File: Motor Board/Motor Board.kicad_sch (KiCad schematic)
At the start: 25 parts, among them J1 Programmer, J2 Gecko, J3 Gecko, J4 Conn_01x02_Socket, J5 Conn_01x02_Socket, Q1 BSS316NN, U2 PIC18F26K83, U3 MCP2562, U4 INA180

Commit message: Finish schematics and footprint assignments
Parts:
- added R6, R7: 10kR, Resistor_SMD:R_0805_2012Metric_Pad1.20x1.40mm_HandSolder, symbol Device:R_US
- J1: footprint Downloaded:GCT_BG300-05-X-X-A_REVC -> Canhw:PinSocket_5x2.54_SMD_90deg_952-3198-1-ND
- J2, J3: footprint Downloaded:G125-MH10605M4R -> Canhw:connector_Harwin_G125–MG10605M4P
- J4, J5: footprint (none) -> Connector_JST:JST_PH_S2B-PH-K_1x02_P2.00mm_Horizontal
- R5: symbol Device:R -> Device:R_US
- U2: footprint Downloaded:SOIC28_SO_MCH -> Package_SO:SOIC-28W_7.5x18.7mm_P1.27mm
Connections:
- net +5V: now also J3.2 (Pin_2), Q1.3 (D)
- net GND: now also J3.5 (Pin_5), Q1.2 (S), R6.2, R7.2
- net LIM_1: now also R6.1
- net LIM_2: now also R7.1
- net MTR_ON: now reaches Q1.1 (G)
- net MTR_ON: now also U2.26 (RB5)
- net MTR_OUT: now reaches J3.3 (Pin_3)
- net MTR_OUT: now also U2.25 (RB4)
- net MTR_IN: now reaches J3.4 (Pin_4)
- net MTR_IN: now also U2.24 (RB3)
- net +12V: no longer names the net of J2.6 (Pin_6)
- no-connect marks 1 -> 12
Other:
- moved on the sheet: J4, J5, Q1

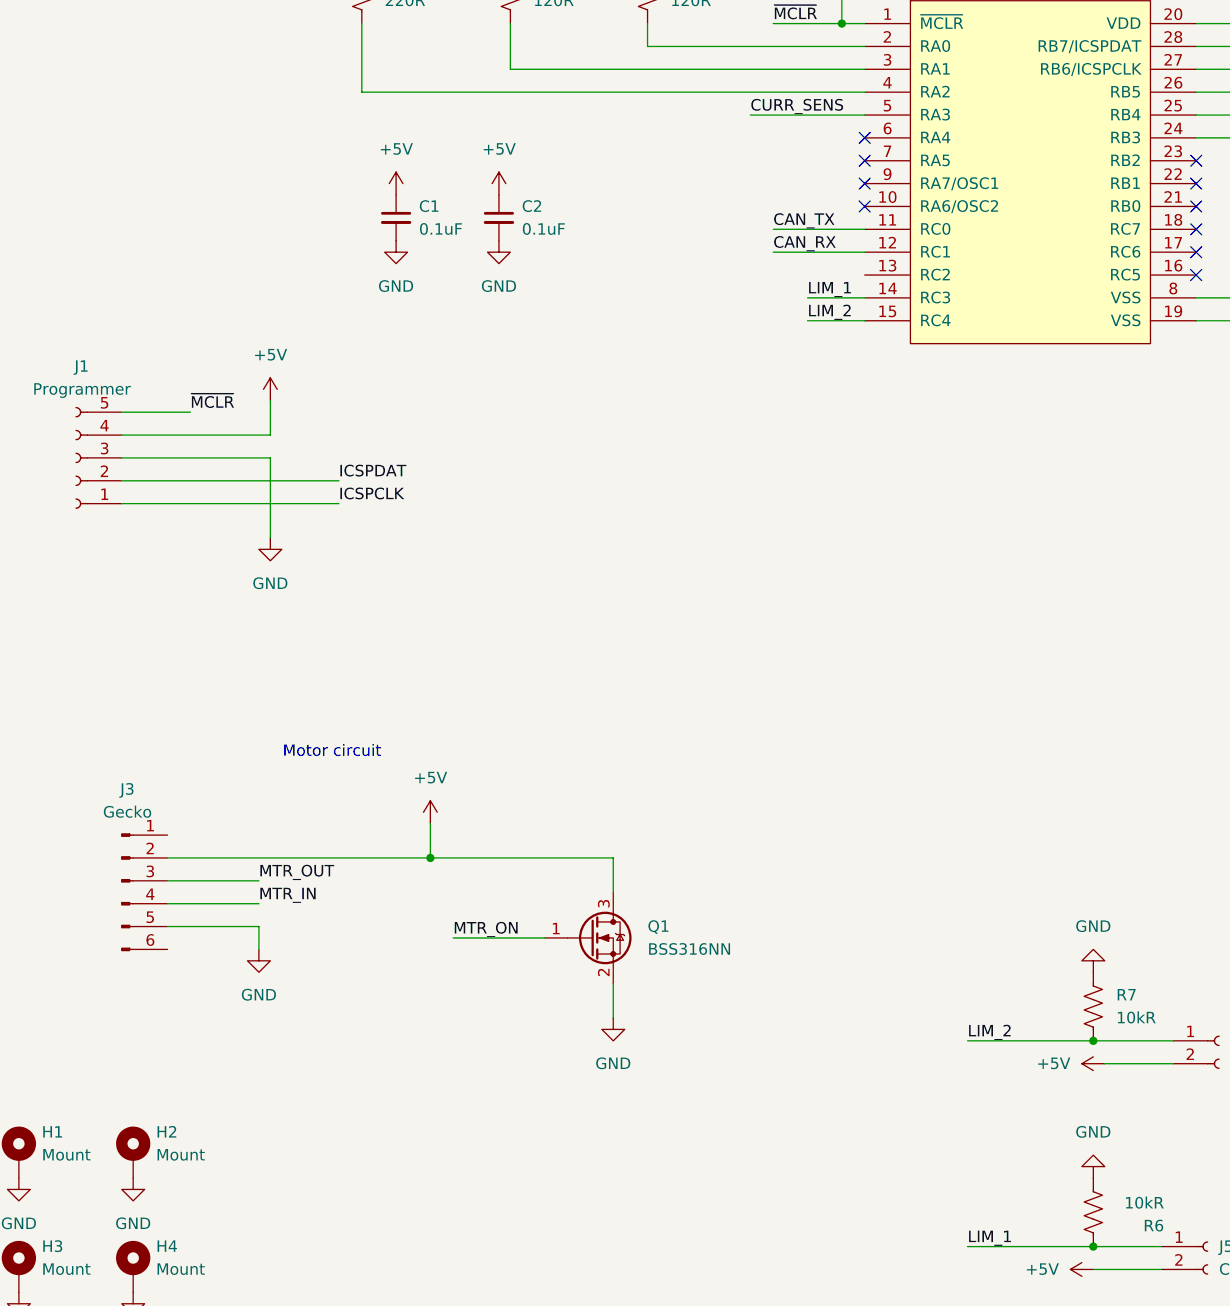
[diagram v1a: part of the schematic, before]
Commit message: Add osc to motor
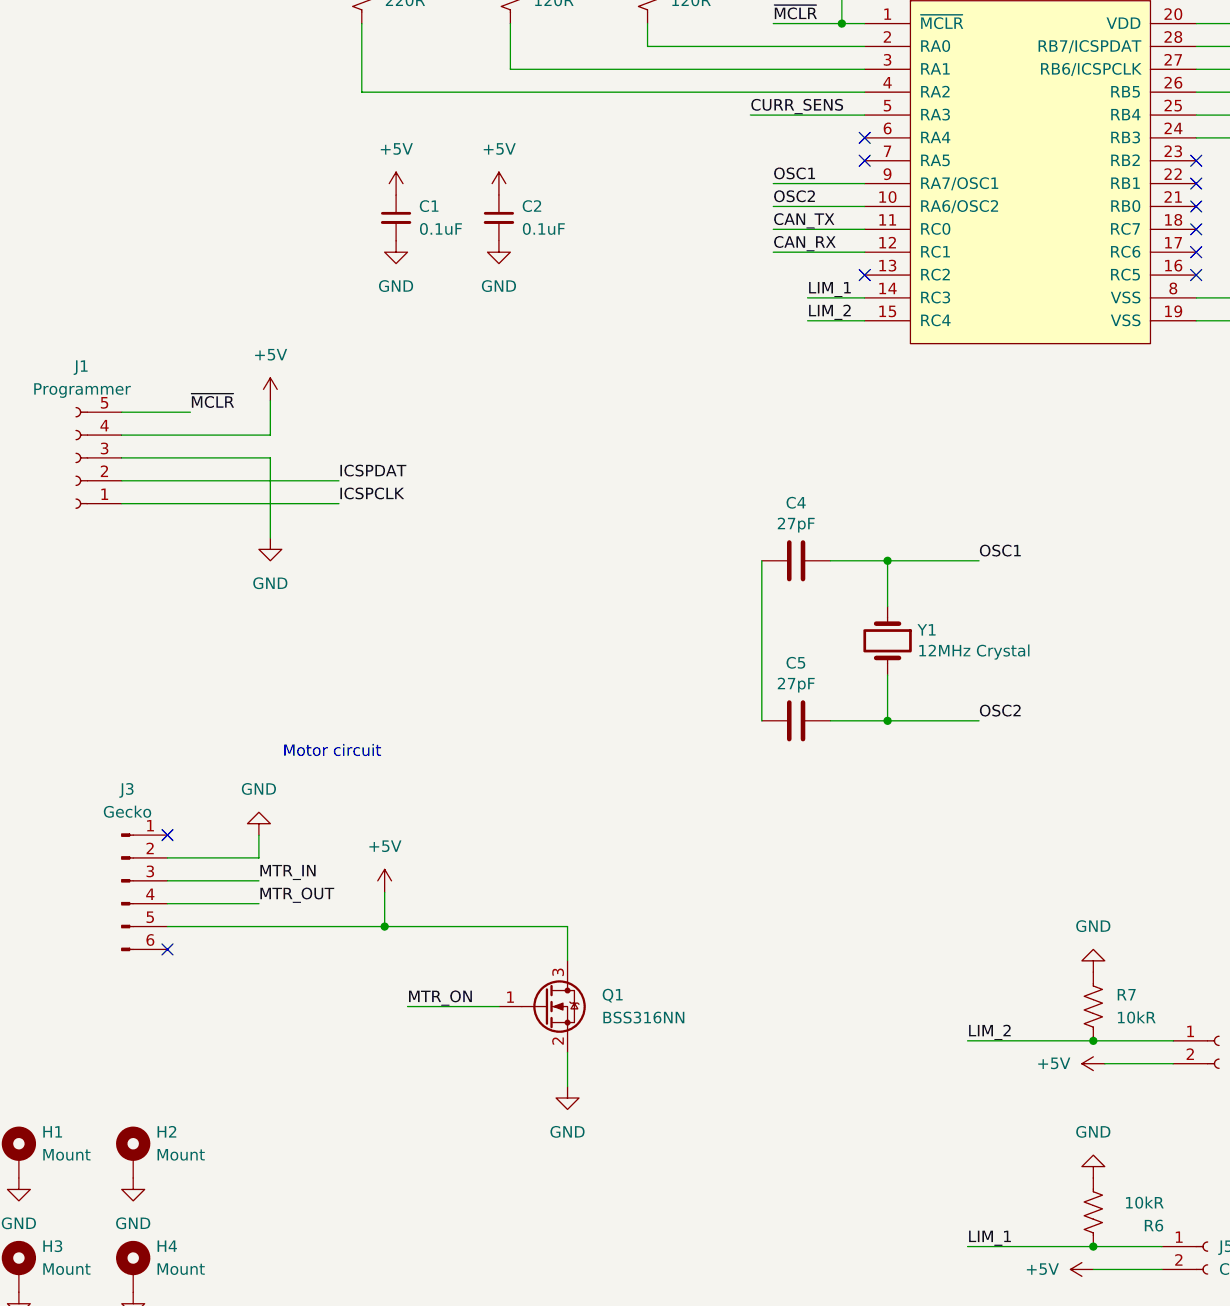
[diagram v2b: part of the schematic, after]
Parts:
- added C4, C5: 27pF, Capacitor_SMD:C_0805_2012Metric_Pad1.18x1.45mm_HandSolder, symbol Device:C
- added Y1: 12MHz Crystal, Crystal:Crystal_HC49-4H_Vertical, symbol Device:Crystal
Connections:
- net +5V: now also J3.5 (Pin_5); no longer J3.2 (Pin_2)
- net GND: now also J3.2 (Pin_2); no longer J3.5 (Pin_5)
- net MTR_IN: now also J3.3 (Pin_3); no longer J3.4 (Pin_4)
- net MTR_OUT: now also J3.4 (Pin_4); no longer J3.3 (Pin_3)
- net OSC2: now reaches U2.10 (RA6/OSC2)
- net OSC2: now also C5.1, Y1.2
- net OSC1: now reaches U2.9 (RA7/OSC1)
- net OSC1: now also C4.1, Y1.1
- new net: C4.2, C5.2
- no-connect marks 12 -> 13
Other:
- moved on the sheet: Q1

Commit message: Push motor
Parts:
- added C6, C7, C8: 10uF, Capacitor_SMD:C_0805_2012Metric_Pad1.18x1.45mm_HandSolder, symbol Device:C
- added R10, R9: 1kR, Resistor_SMD:R_0805_2012Metric_Pad1.20x1.40mm_HandSolder, symbol Device:R_US
- added R8: 10kR, Resistor_SMD:R_0805_2012Metric_Pad1.20x1.40mm_HandSolder, symbol Device:R_US
- added TP1: 5v TP, TestPoint:TestPoint_Pad_1.5x1.5mm, symbol Connector:TestPoint
- added TP2: PWM TP, TestPoint:TestPoint_Pad_1.5x1.5mm, symbol Connector:TestPoint
- added TP3: LIM2 TP, TestPoint:TestPoint_Pad_1.5x1.5mm, symbol Connector:TestPoint
- added TP4: LIM1 TP, TestPoint:TestPoint_Pad_1.5x1.5mm, symbol Connector:TestPoint
- F1: value Polyfuse 350mA -> Polyfuse 750mA
- R5: value 62mR -> 10R
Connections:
- net +5V: now also Q1.2 (S), R6.1, R7.1, C6.1, TP1.1; no longer J3.5 (Pin_5), J4.2 (Pin_2), J5.2 (Pin_2), Q1.3 (D)
- net GND: now also J4.1 (Pin_1), J5.1 (Pin_1), C6.2, C7.2, C8.2, R10.1, R8.2, R9.1; no longer Q1.2 (S), R6.2, R7.2, U3.2 (VSS), U3.8 (STBY)
- net LIM_1: now also C8.1, R10.2, TP4.1; no longer J5.1 (Pin_1), R6.1
- net LIM_2: now also C7.1, R9.2, TP3.1; no longer J4.1 (Pin_1), R7.1
- net MTR_IN: now also TP2.1
- net MTR_ON: now also R8.1
- new net: J4.2 (Pin_2), R7.2
- new net: J3.5 (Pin_5), Q1.3 (D)
- new net: U3.2 (VSS), U3.8 (STBY)
- new net: J5.2 (Pin_2), R6.2
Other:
- note added: "FITEC FS90R"
- note added: "RC acts as bounce filter with cutoff around 20Hz"
- note added: "max = 500mA"
- moved on the sheet: J4, J5, R7

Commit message: Fix review items
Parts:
- F1: value Polyfuse 750mA -> Polyfuse 1.5A
- R5: value 10R -> 50mR
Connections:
- net +5V: now also J4.2 (Pin_2), J5.2 (Pin_2); no longer R6.1, R7.1
- net GND: now also C4.2, C5.2, R6.2, R7.2; no longer J4.1 (Pin_1), J5.1 (Pin_1), R10.1, R9.1
- net LIM_1: now also R6.1
- net LIM_2: now also R7.1
- net MTR_OUT: no longer names the net of J3.4 (Pin_4)
- net MTR_OUT: no longer U2.25 (RB4)
- new net: J5.1 (Pin_1), R10.1
- new net: J4.1 (Pin_1), R9.1
- no-connect marks 13 -> 15
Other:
- note added: "max = 1A"
- note removed: "max = 500mA"
- moved on the sheet: TP1, TP2, TP3, TP4

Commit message: Forgot to push, fix mosfets
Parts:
- removed C1, C2: 0.1uF, Capacitor_SMD:C_0805_2012Metric_Pad1.18x1.45mm_HandSolder, symbol Device:C_Small
- added C1: 0.1uF, Capacitor_SMD:C_0805_2012Metric_Pad1.18x1.45mm_HandSolder, symbol Device:C
- added Q2: DMG2305UX-7, Package_TO_SOT_SMD:SOT-23, symbol Device:Q_PMOS_SGD
- added R11: 10kR, Resistor_SMD:R_0805_2012Metric_Pad1.20x1.40mm_HandSolder, symbol Device:R_US
- added R12: 120R, Resistor_SMD:R_0805_2012Metric_Pad1.20x1.40mm_HandSolder, symbol Device:R_US
- Q1: footprint Package_TO_SOT_SMD:SOT-323_SC-70 -> Package_TO_SOT_SMD:SOT-323_SC-70_Handsoldering
- renumbered C3 to C2, C4 to C3, C5 to C4, C6 to C5, C7 to C6, C8 to C7
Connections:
- net +5V: now also R8.1, C1.1, Q2.1 (S); no longer Q1.2 (S)
- net GND: now also Q1.2 (S), U3.2 (VSS), U3.8 (STBY), C1.2, R11.2; no longer R8.2
- net MTR_ON: now also R12.1; no longer Q1.1 (G), R8.1
- net at Q1.3 (D): now also R8.2, Q2.2 (G); no longer J3.5 (Pin_5)
- new net: Q1.1 (G), R11.1, R12.2
- new net: J3.5 (Pin_5), Q2.3 (D)
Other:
- moved on the sheet: C3, C4, J1, J3, Q1, TP1, TP2, TP3, TP4, Y1

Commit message: redit layout
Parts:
- J1: footprint Canhw:PinSocket_5x2.54_SMD_90deg_952-3198-1-ND -> canhw:PinSocket_5x2.54_SMD_90deg_952-3198-1-ND
- J2, J3: footprint Canhw:connector_Harwin_G125–MG10605M4P -> canhw:connector_Harwin_G125–MG10605M4P
- Y1: value 12MHz Crystal -> 12MHz Crystal
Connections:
- net CURR_SENS: now also U2.16 (RC5); no longer U2.5 (RA3)
- net LIM_1: now also U2.22 (RB1); no longer U2.14 (RC3)
- net LIM_2: now also U2.23 (RB2); no longer U2.15 (RC4)
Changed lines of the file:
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@@
 	)
 	(no_connect
-		(at 147.32 77.47)
+		(at 110.49 59.69)
 	)
 	(no_connect
@@
 	)
 	(no_connect
-		(at 147.32 67.31)
+		(at 147.32 72.39)
 	)
 	(no_connect
-		(at 147.32 72.39)
+		(at 110.49 80.01)
 	)
 	(no_connect
@@
 	)
 	(no_connect
+		(at 110.49 82.55)
+	)
+	(no_connect
 		(at 147.32 74.93)
 	)
@@
 		(at 22.86 109.22)
 	)
-	(no_connect
-		(at 147.32 64.77)
-	)
 	(wire
 		(pts
@@
 	(wire
 		(pts
-			(xy 104.14 82.55) (xy 110.49 82.55)
-		)
-		(stroke
-			(width 0)
-			(type default)
-		)
-	)
-	(wire
-		(pts
 			(xy 100.33 158.75) (xy 104.14 158.75)
 		)
@@
 	(wire
 		(pts
-			(xy 104.14 80.01) (xy 110.49 80.01)
-		)
-		(stroke
-			(width 0)
-			(type default)
-		)
-	)
-	(wire
-		(pts
 			(xy 110.49 52.07) (xy 86.36 52.07)
 		)
@@
 	(wire
 		(pts
-			(xy 97.79 59.69) (xy 110.49 59.69)
-		)
-		(stroke
-			(width 0)
-			(type default)
-		)
-	)
-	(wire
-		(pts
 			(xy 104.14 151.13) (xy 104.14 158.75)
 		)
@@
 	(label "CAN_RX"
 		(at 100.33 74.93 0)
-		(fields_autoplaced yes)
 		(effects
 			(font
@@
 	(label "ICSPCLK"
 		(at 156.21 54.61 0)
-		(fields_autoplaced yes)
 		(effects
 			(font
@@
 	(label "LIM_2"
 		(at 231.14 31.75 0)
-		(fields_autoplaced yes)
 		(effects
 			(font
@@
 	(label "CANL"
 		(at 236.22 63.5 180)
-		(fields_autoplaced yes)
 		(effects
 			(font
@@
 	(label "CAN_TX"
 		(at 100.33 72.39 0)
-		(fields_autoplaced yes)
 		(effects
 			(font
@@
 	(label "MTR_IN"
 		(at 156.21 62.23 0)
-		(fields_autoplaced yes)
 		(effects
 			(font
@@
 	(label "MTR_ON"
 		(at 16.51 135.89 0)
-		(fields_autoplaced yes)
 		(effects
 			(font
@@
 	(label "MTR_IN"
 		(at 33.02 114.3 0)
-		(fields_autoplaced yes)
 		(effects
 			(font
@@
 	(label "CANH"
 		(at 236.22 60.96 180)
-		(fields_autoplaced yes)
 		(effects
 			(font
@@
 	(label "CANH"
 		(at 203.2 105.41 0)
-		(fields_autoplaced yes)
 		(effects
 			(font
@@
 	(label "OSC1"
 		(at 143.51 102.87 0)
-		(fields_autoplaced yes)
 		(effects
 			(font
@@
 	(label "OSC2"
 		(at 100.33 69.85 0)
-		(fields_autoplaced yes)
 		(effects
 			(font
@@
 	(label "OSC1"
 		(at 100.33 67.31 0)
-		(fields_autoplaced yes)
 		(effects
 			(font
@@
 	(label "OSC2"
 		(at 143.51 120.65 0)
-		(fields_autoplaced yes)
 		(effects
 			(font
@@
 	(label "LIM_1"
 		(at 250.19 31.75 0)
-		(fields_autoplaced yes)
 		(effects
 			(font
@@
 	(label "LIM_1"
 		(at 104.14 175.26 0)
-		(fields_autoplaced yes)
 		(effects
 			(font
@@
 	(label "LIM_2"
 		(at 104.14 151.13 0)
-		(fields_autoplaced yes)
 		(effects
 			(font
@@
 	(label "ICSPCLK"
 		(at 50.8 81.28 0)
-		(fields_autoplaced yes)
 		(effects
 			(font
@@
 	(label "ICSPDAT"
 		(at 50.8 78.74 0)
-		(fields_autoplaced yes)
 		(effects
 			(font
@@
 	(label "MTR_IN"
 		(at 207.01 31.75 0)
-		(fields_autoplaced yes)
 		(effects
 			(font
@@
 	(label "CAN_TX"
 		(at 189.23 63.5 0)
-		(fields_autoplaced yes)
 		(effects
 			(font
@@
 	)
 	(label "LIM_1"
-		(at 104.14 80.01 0)
-		(fields_autoplaced yes)
+		(at 147.32 67.31 0)
 		(effects
 			(font
@@
 	(label "MTR_ON"
 		(at 156.21 57.15 0)
-		(fields_autoplaced yes)
 		(effects
 			(font
@@
 	(label "~{MCLR}"
 		(at 34.29 71.12 0)
-		(fields_autoplaced yes)
 		(effects
 			(font
@@
 	(label "CAN_RX"
 		(at 189.23 66.04 0)
-		(fields_autoplaced yes)
 		(effects
 			(font
@@
 	)
 	(label "LIM_2"
-		(at 104.14 82.55 0)
-		(fields_autoplaced yes)
+		(at 147.32 64.77 0)
 		(effects
 			(font
@@
 	(label "~{MCLR}"
 		(at 100.33 49.53 0)
-		(fields_autoplaced yes)
 		(effects
 			(font
@@
 	)
 	(label "CURR_SENS"
-		(at 97.79 59.69 0)
-		(fields_autoplaced yes)
+		(at 147.32 77.47 0)
 		(effects
 			(font
@@
 	(label "ICSPDAT"
 		(at 156.21 52.07 0)
-		(fields_autoplaced yes)
 		(effects
 			(font
@@
 	(label "CURR_SENS"
 		(at 267.97 134.62 0)
-		(fields_autoplaced yes)
 		(effects
 			(font
@@
 	(label "CANL"
 		(at 203.2 102.87 0)
-		(fields_autoplaced yes)
 		(effects
 			(font
@@
 			)
 		)
-		(property "Value" "12MHz Crystal "
+		(property "Value" "12MHz Crystal"
 			(at 136.6774 112.903 90)
 			(effects
@@
 			)
 		)
-		(property "Footprint" "Canhw:PinSocket_5x2.54_SMD_90deg_952-3198-1-ND"
+		(property "Footprint" "canhw:PinSocket_5x2.54_SMD_90deg_952-3198-1-ND"
 			(at 21.59 76.2 0)
 			(effects
@@
 			)
 		)
-		(property "Footprint" "Canhw:connector_Harwin_G125–MG10605M4P"
+		(property "Footprint" "canhw:connector_Harwin_G125–MG10605M4P"
 			(at 17.78 114.3 0)
 			(effects
@@
 			)
 		)
-		(property "Footprint" "Canhw:connector_Harwin_G125–MG10605M4P"
+		(property "Footprint" "canhw:connector_Harwin_G125–MG10605M4P"
 			(at 185.42 105.41 0)
 			(effects
